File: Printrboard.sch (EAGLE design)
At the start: 122 parts, among them J1 MICROSD, J3 ATX, Q1 RFP30N06LE, Q2 RFP30N06LE, Q3 RFP30N06LE, U1 LM2841, U2 A4982, U3 A4982, U4 A4982, U5 A4982, U6 AT90USB1286, U7 AP7313, U8 TXB0104, X1 16MHz, X2 USB-MICROB

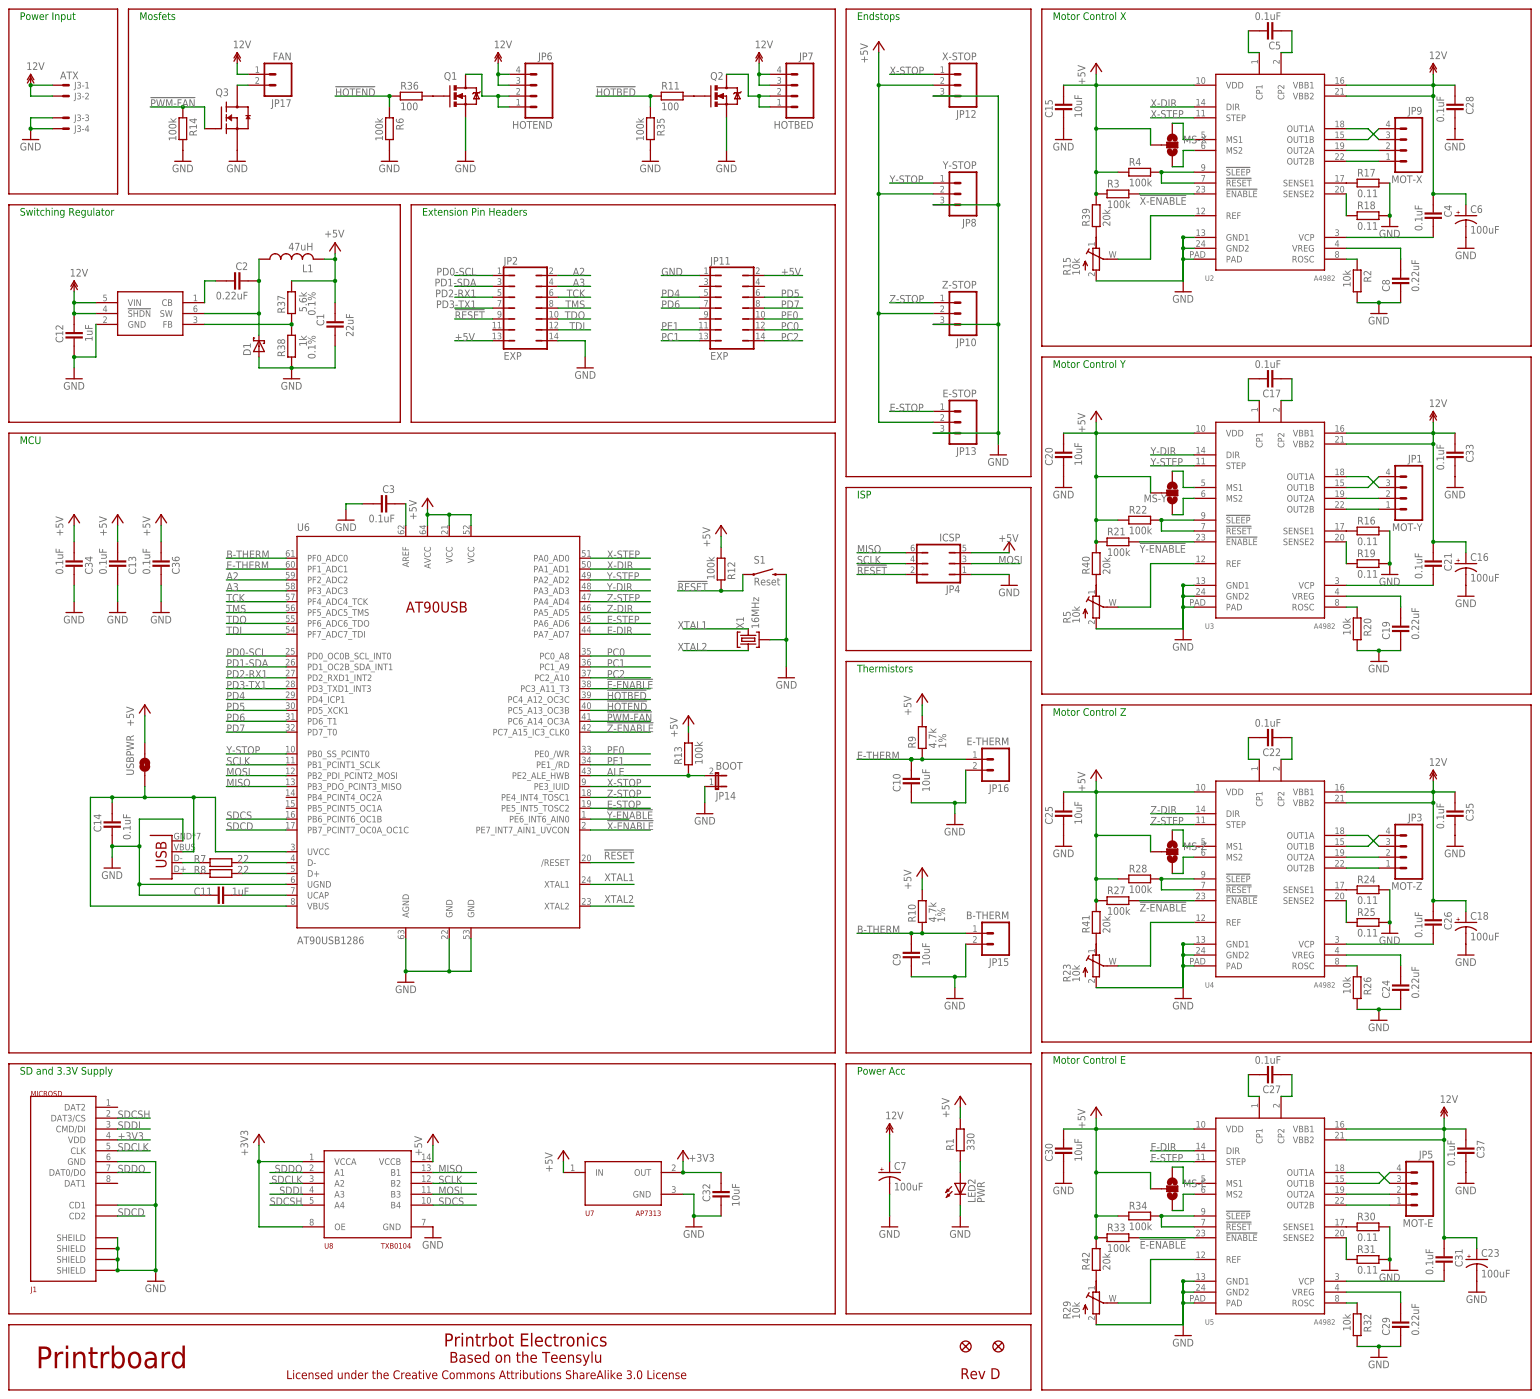
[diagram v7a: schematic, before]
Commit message: Update files for Rev F
Changed heatbed connector to 5mm pitch screw terminal
Removed E-STOP connector
Changed Y-STOP pin
Moved former Y-STOP pin to SD interface to fix a limitation of the SPI ctlr
Added I2C connector
Replaced trimpots with 4-channel I2C DAC
Added polyfuse and reverse protection diode to fan circuit
Added more empty space around fan connector
Made ICSP and EXP1 connector pins share a 0.1" grid
Removed reset signal from EXP1, and replaced it with GPIO
Changed input PWR connector to a 6-pin one from the same family
Removed stop layer from several vias for future bed-of-nails tester
Change to through-hole mount microUSB connector
Added USB TVS diode pack to protect USB controller from ESD
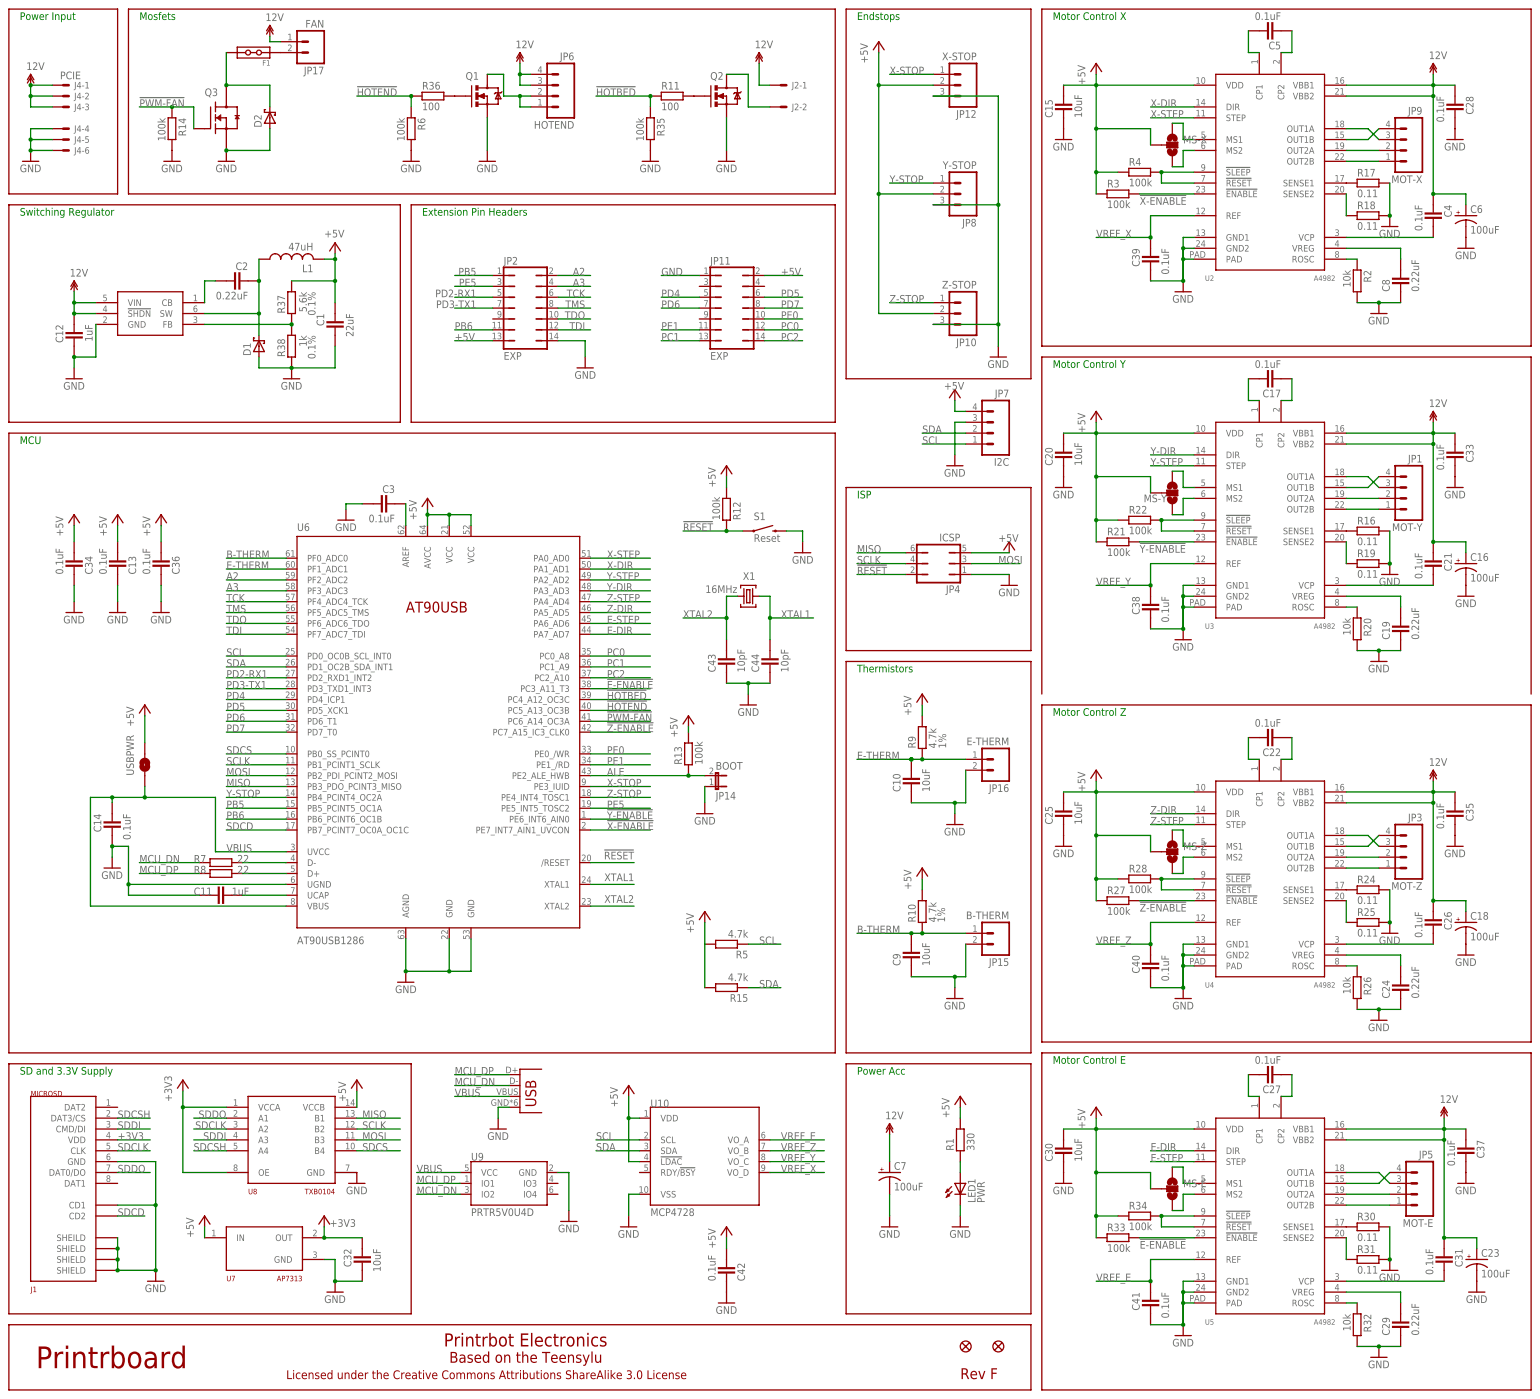
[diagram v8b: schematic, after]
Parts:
- removed JP13: E-STOP, SparkFun:M03POLAR
- removed R23, R29: 10k, printrbot:RTRIM-ST-4EA
- removed R39, R40, R41, R42: 20k, ipc-7351-resistor:RESISTOR_0805
- removed X2: USB-MICROB, printrbot:USB-MICROB
- added C38, C39, C40, C41, C42: 0.1uF, ipc-7351-capacitor:CAPACITOR_0805
- added C43, C44: 10pF, ipc-7351-capacitor:CAPACITOR_0805
- added D2: SCH-DIODESMA, printrbot:SCH-DIODESMA
- added F1: MINISMDC050F, printrbot:MINISMDC050F
- added J2: (no value), printrbot:PHOENIX-2POS-5MM-SCREW
- added J4: PCIE, printrbot:5566-6
- added U10: MCP4728, printrbot:MCP4728
- added U9: PRTR5V0U4D, printrbot:PRTR5V0U4D
- J3: value ATX -> USB-MICRO-PTH; device printrbot:5566-4 -> printrbot:USB-MICRO-PTH
- JP7: value HOTBED -> I2C
- R15, R5: value 10k -> 4.7k; device printrbot:RTRIM-ST-4EA -> ipc-7351-resistor:RESISTOR_0805
- X1: device printrbot:AWSCR-CV -> printrbot:XTAL
- renumbered LED2 to LED1
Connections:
- removed net E-STOP: JP13.1, U6.PE5_INT5_TOSC2
- removed net N$18: R15.S, U2.REF
- removed net N$33: R5.S, U3.REF
- removed net N$48: R23.S, U4.REF
- removed net N$6: JP17.2, Q3.D
- removed net N$63: R29.S, U5.REF
- removed net N$69: R15.A, R39.1
- removed net N$74: R29.A, R42.1
- removed net N$78: R23.A, R41.1
- removed net N$8: R40.1, R5.A
- removed net PD0-SCL: JP2.1, U6.PD0_OC0B_SCL_INT0
- removed net PD1-SDA: JP2.3, U6.PD1_OC2B_SDA_INT1
- new net MCU_DN: J3.D-, R7.1, U9.IO2
- new net MCU_DP: J3.D+, R8.1, U9.IO1
- new net PB5: JP2.1, U6.PB5_PCINT5_OC1A
- new net PB6: JP2.11, U6.PB6_PCINT6_OC1B
- new net PE5: JP2.3, U6.PE5_INT5_TOSC2
- new net SCL: JP7.1, R5.1, U10.SCL, U6.PD0_OC0B_SCL_INT0
- new net SDA: JP7.2, R15.1, U10.SDA, U6.PD1_OC2B_SDA_INT1
- new net VREF_E: C41.1, U10.VO_A, U5.REF
- new net VREF_X: C39.1, U10.VO_D, U2.REF
- new net VREF_Y: C38.1, U10.VO_C, U3.REF
- new net VREF_Z: C40.1, U10.VO_B, U4.REF
- net !RESET: no longer JP2.9
- net +5V: now also C42.2, JP7.4, R15.2, R5.2, U10.!LDAC, U10.VDD; no longer JP13.2, R39.2, R40.2, R41.2, R42.2
- net 12V: now also J2-1.S, J4-1.S, J4-2.S, J4-3.S; no longer J3-1.S, J3-2.S, JP7.3, JP7.4
- net GND: now also C38.2, C39.2, C40.2, C41.2, C42.1, C43.1, C44.1, D2.A, J3.GND, J4-4.S, J4-5.S, J4-6.S, JP7.3, U10.VSS, U9.GND; no longer J3-3.S, J3-4.S, JP13.3, R15.E, R23.E, R29.E, R5.E, X1.2, X2.GND
- net HOTBED-GND: now also J2-2.S; no longer JP7.1, JP7.2
- net N$2: now also D2.C, F1.P$2, Q3.D; no longer R7.1, X2.D-
- net N$5: now also F1.P$1, JP17.2; no longer R8.1, X2.D+
- net SDCS: now also U6.PB0_SS_PCINT0; no longer U6.PB6_PCINT6_OC1B
- net VBUS: now also J3.VBUS, U9.VCC; no longer X2.VBUS
- net XTAL1: now also C44.2, X1.1; no longer X1.3
- net XTAL2: now also C43.2, X1.2; no longer X1.1
- net Y-STOP: now also U6.PB4_PCINT4_OC2A; no longer U6.PB0_SS_PCINT0
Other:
- note added: "Rev F"
- note removed: "Rev D"
- moved on the sheet: C32, JP17, JP6, JP7, Q1, Q3, R12, R14, R36, R6, S1, U7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
